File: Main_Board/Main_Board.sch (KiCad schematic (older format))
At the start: 67 parts, among them J1 Conn_01x06, J10 HR-SR04_L_CONN, J11 12V_OUT, J12 BATT_REG_IN, J13 LED_CONN, J14 PD_CONN, J2 Conn_01x06, J3 Conn_01x06, J4 BATT_IN, J5 Conn_02x08_Top_Bottom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

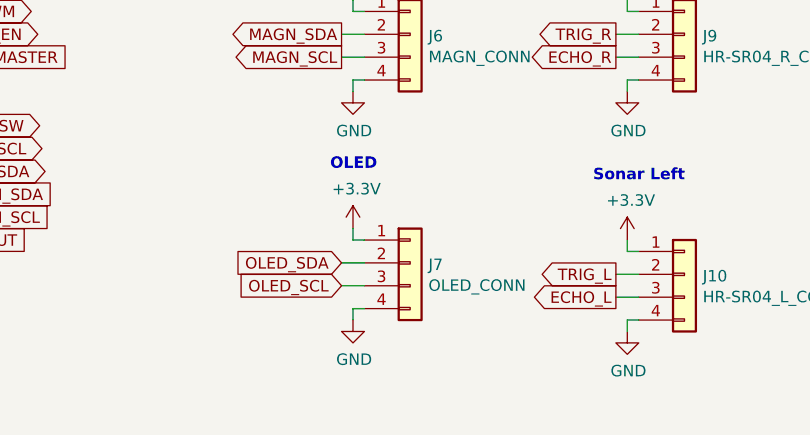
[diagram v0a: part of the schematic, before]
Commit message: Small changes to 12V connector [MAIN BOARD]
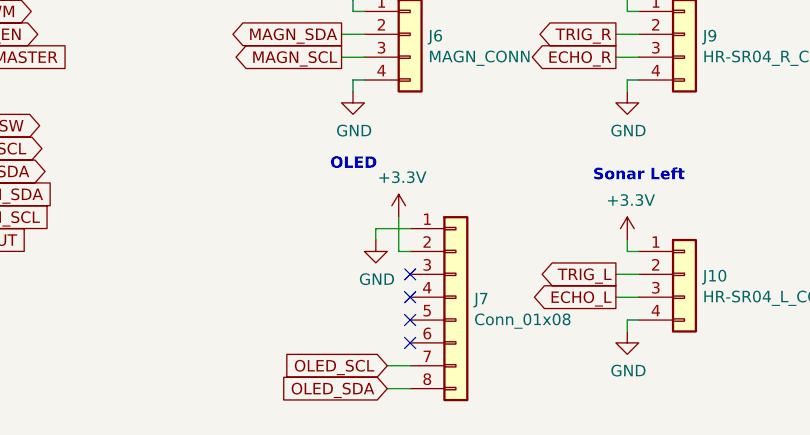
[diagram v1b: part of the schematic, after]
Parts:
- removed J7: OLED_CONN, Connector_PinSocket_2.54mm:PinSocket_1x04_P2.54mm_Vertical, symbol Connector_Generic:Conn_01x04
- added J7: Conn_01x08, symbol Connector_Generic:Conn_01x08
- J11, J12: footprint Connector_Molex:Molex_Mini-Fit_Jr_5566-04A_2x02_P4.20mm_Vertical -> Main_Board:215760-YY04
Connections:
- net +3V3: now also J7.2 (Pin_2)
- net GND: now also J7.1 (Pin_1)
- net OLED_SCL: now also J7.7 (Pin_7)
- net OLED_SDA: now also J7.8 (Pin_8)
- no-connect marks 93 -> 97
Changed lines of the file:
@@
-	1    0    0    -1
-$EndComp
-$Comp
-L Connector_Generic:Conn_01x04 J7
-U 1 1 61EF5837
-P 8500 10200
-F 0 "J7" H 8580 10192 50  0000 L CNN
-F 1 "OLED_CONN" H 8580 10101 50  0000 L CNN
-F 2 "Connector_PinSocket_2.54mm:PinSocket_1x04_P2.54mm_Vertical" H 8500 10200 50  0001 C CNN
-F 3 "~" H 8500 10200 50  0001 C CNN
-	1    8500 10200
 	1    0    0    -1
 $EndComp
@@
 Text GLabel 4550 8400 0    50   Output ~ 0
 LED_DIN
-Text GLabel 8200 10200 0    50   Input ~ 0
+Text GLabel 8400 10750 0    50   Input ~ 0
 OLED_SDA
-Text GLabel 8200 10300 0    50   Input ~ 0
+Text GLabel 8400 10650 0    50   Input ~ 0
 OLED_SCL
 Wire Wire Line
-	8200 10200 8300 10200
-Wire Wire Line
-	8200 10300 8300 10300
-Wire Wire Line
-	8250 10050 8250 10100
-Wire Wire Line
-	8250 10100 8300 10100
+	8400 10750 8500 10750
+Wire Wire Line
+	8400 10650 8500 10650
 $Comp
 L power:GND #PWR021
 U 1 1 620F9588
-P 8250 10450
-F 0 "#PWR021" H 8250 10200 50  0001 C CNN
-F 1 "GND" H 8255 10277 50  0000 C CNN
-F 2 "" H 8250 10450 50  0001 C CNN
-F 3 "" H 8250 10450 50  0001 C CNN
-	1    8250 10450
-	1    0    0    -1
-$EndComp
-Wire Wire Line
-	8250 10450 8250 10400
-Wire Wire Line
-	8250 10400 8300 10400
+P 8350 10100
+F 0 "#PWR021" H 8350 9850 50  0001 C CNN
+F 1 "GND" H 8355 9927 50  0000 C CNN
+F 2 "" H 8350 10100 50  0001 C CNN
+F 3 "" H 8350 10100 50  0001 C CNN
+	1    8350 10100
+	1    0    0    -1
+$EndComp
+Wire Wire Line
+	8350 10100 8350 10050
+Wire Wire Line
+	8350 10050 8500 10050
 Text GLabel 8200 9200 0    50   Output ~ 0
 MAGN_SDA
@@
 L power:+3.3V #PWR020
 U 1 1 62001B8E
-P 8250 10050
-F 0 "#PWR020" H 8250 9900 50  0001 C CNN
-F 1 "+3.3V" H 8265 10223 50  0000 C CNN
-F 2 "" H 8250 10050 50  0001 C CNN
-F 3 "" H 8250 10050 50  0001 C CNN
-	1    8250 10050
+P 8450 10000
+F 0 "#PWR020" H 8450 9850 50  0001 C CNN
+F 1 "+3.3V" H 8465 10173 50  0000 C CNN
+F 2 "" H 8450 10000 50  0001 C CNN
+F 3 "" H 8450 10000 50  0001 C CNN
+	1    8450 10000
 	1    0    0    -1
 $EndComp
@@
 F 0 "J11" H 7750 2000 50  0000 L CNN
 F 1 "12V_OUT" H 7650 1700 50  0000 L CNN
-F 2 "Connector_Molex:Molex_Mini-Fit_Jr_5566-04A_2x02_P4.20mm_Vertical" H 7800 1900 50  0001 C CNN
+F 2 "Main_Board:215760-YY04" H 7800 1900 50  0001 C CNN
 F 3 "~" H 7800 1900 50  0001 C CNN
 	1    7800 1900
@@
 F 0 "J12" H 8200 1700 50  0000 L CNN
 F 1 "BATT_REG_IN" H 8100 2000 50  0000 L CNN
-F 2 "Connector_Molex:Molex_Mini-Fit_Jr_5566-04A_2x02_P4.20mm_Vertical" H 8250 1900 50  0001 C CNN
+F 2 "Main_Board:215760-YY04" H 8250 1900 50  0001 C CNN
 F 3 "~" H 8250 1900 50  0001 C CNN
 	1    8250 1900
@@
 Wire Wire Line
 	12100 8150 12200 8150
+$Comp
+L Connector_Generic:Conn_01x08 J7
+U 1 1 6204F2B5
+P 8700 10350
+F 0 "J7" H 8780 10342 50  0000 L CNN
+F 1 "Conn_01x08" H 8780 10251 50  0000 L CNN
+F 2 "" H 8700 10350 50  0001 C CNN
+F 3 "~" H 8700 10350 50  0001 C CNN
+	1    8700 10350
+	1    0    0    -1
+$EndComp
+NoConn ~ 8500 10550
+NoConn ~ 8500 10450
+NoConn ~ 8500 10350
+NoConn ~ 8500 10250
+Wire Wire Line
+	8500 10150 8450 10150
+Wire Wire Line
+	8450 10150 8450 10000
 $EndSCHEMATC

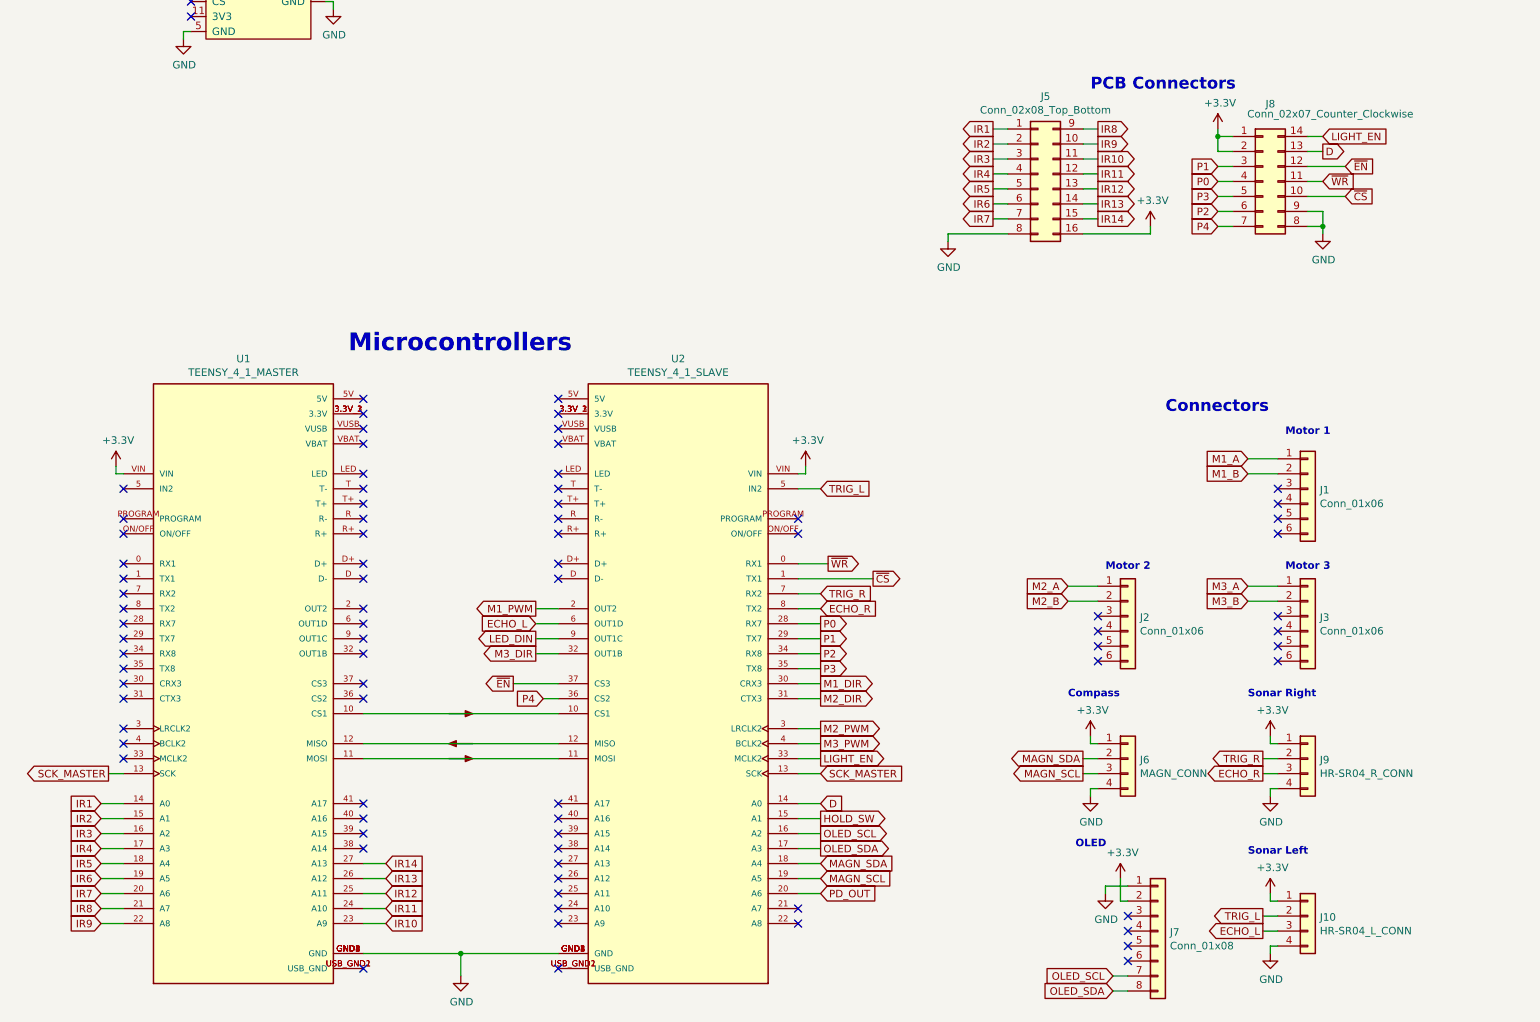
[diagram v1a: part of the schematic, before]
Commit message: Started actual traces [MAIN BOARD]
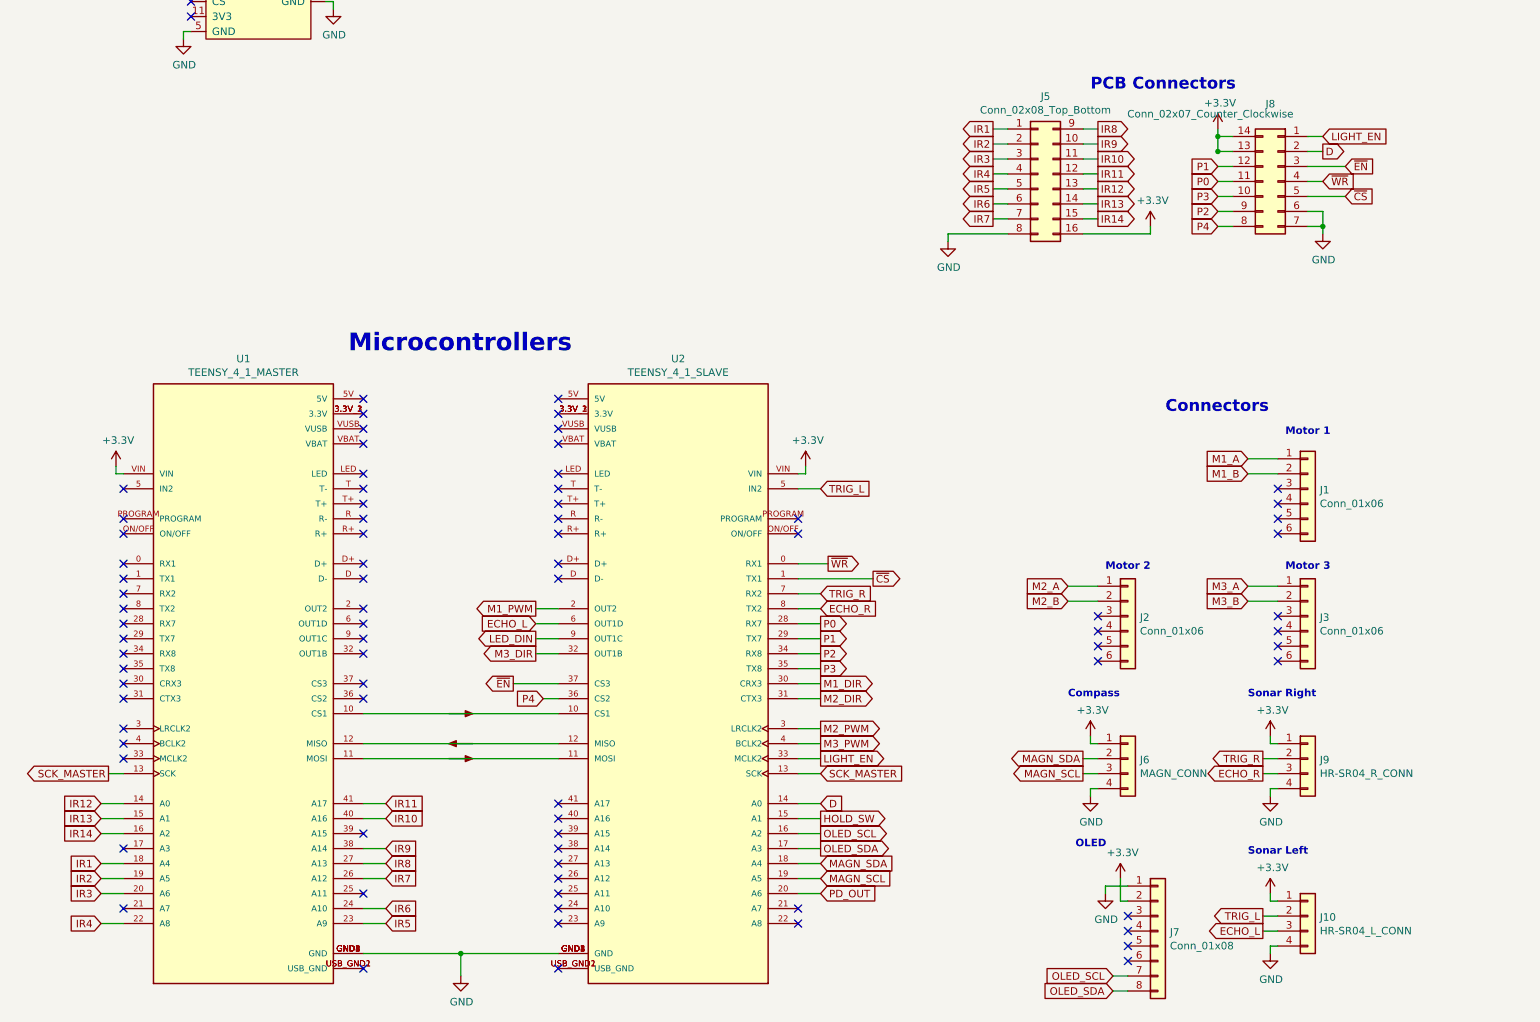
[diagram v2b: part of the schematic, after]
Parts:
- J7: footprint (none) -> Connector_PinSocket_2.54mm:PinSocket_1x08_P2.54mm_Vertical
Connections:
- net +3V3: now also J8.13 (Pin_13), J8.14 (Pin_14); no longer J8.1 (Pin_1), J8.2 (Pin_2)
- net D: now also J8.2 (Pin_2); no longer J8.13 (Pin_13)
- net GND: now also J8.6 (Pin_6), J8.7 (Pin_7); no longer J8.8 (Pin_8), J8.9 (Pin_9)
- net IR1: now also U1.18 (A4); no longer U1.14 (A0)
- net IR10: now also U1.40 (A16); no longer U1.23 (A9)
- net IR11: now also U1.41 (A17); no longer U1.24 (A10)
- net IR12: now also U1.14 (A0); no longer U1.25 (A11)
- net IR13: now also U1.15 (A1); no longer U1.26 (A12)
- net IR14: now also U1.16 (A2); no longer U1.27 (A13)
- net IR2: now also U1.19 (A5); no longer U1.15 (A1)
- net IR3: now also U1.20 (A6); no longer U1.16 (A2)
- net IR4: now also U1.22 (A8); no longer U1.17 (A3)
- net IR5: now also U1.23 (A9); no longer U1.18 (A4)
- net IR6: now also U1.24 (A10); no longer U1.19 (A5)
- net IR7: now also U1.26 (A12); no longer U1.20 (A6)
- net IR8: now also U1.27 (A13); no longer U1.21 (A7)
- net IR9: now also U1.38 (A14); no longer U1.22 (A8)
- net LIGHT_EN: now also J8.1 (Pin_1); no longer J8.14 (Pin_14)
- net P0: now also J8.11 (Pin_11); no longer J8.4 (Pin_4)
- net P1: now also J8.12 (Pin_12); no longer J8.3 (Pin_3)
- net P2: now also J8.9 (Pin_9); no longer J8.6 (Pin_6)
- net P3: now also J8.10 (Pin_10); no longer J8.5 (Pin_5)
- net P4: now also J8.8 (Pin_8); no longer J8.7 (Pin_7)
- net ~CS: now also J8.5 (Pin_5); no longer J8.10 (Pin_10)
- net ~EN: now also J8.3 (Pin_3); no longer J8.12 (Pin_12)
- net ~WR: now also J8.4 (Pin_4); no longer J8.11 (Pin_11)
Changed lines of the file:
@@
 Wire Wire Line
 	4700 10500 4050 10500
-$Comp
-L TEENSY_4_1:TEENSY_4_1 U1
-U 1 1 61B35EEE
-P 2600 8700
-F 0 "U1" H 2600 10867 50  0000 C CNN
-F 1 "TEENSY_4_1_MASTER" H 2600 10776 50  0000 C CNN
-F 2 "Main_Board:TEENSY_4_1_FP" H 2600 8700 50  0001 L BNN
-F 3 "" H 2600 8700 50  0001 L BNN
-F 4 "Manufacturer recommendations" H 2600 8700 50  0001 L BNN "STANDARD"
-F 5 "4.07mm" H 2600 8700 50  0001 L BNN "MAXIMUM_PACKAGE_HEIGHT"
-F 6 "4.1" H 2600 8700 50  0001 L BNN "PARTREV"
-F 7 "SparkFun Electronics" H 2600 8700 50  0001 L BNN "MANUFACTURER"
-	1    2600 8700
-	1    0    0    -1
-$EndComp
 Wire Wire Line
 	6300 7300 6350 7300
@@
 NoConn ~ 3400 7100
 NoConn ~ 4700 7100
-$Comp
-L Connector_Generic:Conn_02x07_Counter_Clockwise J8
-U 1 1 62B05C9E
-P 9400 5350
-F 0 "J8" H 9450 5867 50  0000 C CNN
-F 1 "Conn_02x07_Counter_Clockwise" H 9850 5800 50  0000 C CNN
-F 2 "Connector_Hirose:Hirose_DF11-14DP-2DSA_2x07_P2.00mm_Vertical" H 9400 5350 50  0001 C CNN
-F 3 "~" H 9400 5350 50  0001 C CNN
-	1    9400 5350
-	1    0    0    -1
-$EndComp
 Text GLabel 9100 5350 0    50   Input ~ 0
 P0
@@
 Wire Wire Line
 	6450 8200 6300 8200
+Text GLabel 1650 9700 0    50   Input ~ 0
+IR14
+Text GLabel 1650 9600 0    50   Input ~ 0
+IR13
+Text GLabel 1650 9500 0    50   Input ~ 0
+IR12
+Text GLabel 3550 9500 2    50   Input ~ 0
+IR11
+Text GLabel 3550 9600 2    50   Input ~ 0
+IR10
+Text GLabel 3550 9800 2    50   Input ~ 0
+IR9
 Text GLabel 3550 9900 2    50   Input ~ 0
-IR14
+IR8
 Text GLabel 3550 10000 2    50   Input ~ 0
-IR13
-Text GLabel 3550 10100 2    50   Input ~ 0
-IR12
+IR7
 Text GLabel 3550 10200 2    50   Input ~ 0
-IR11
+IR6
 Text GLabel 3550 10300 2    50   Input ~ 0
-IR10
-Text GLabel 1650 10300 0    50   Input ~ 0
-IR9
-Text GLabel 1650 10200 0    50   Input ~ 0
-IR8
+IR5
 Text GLabel 1650 10100 0    50   Input ~ 0
-IR7
+IR3
 Text GLabel 1650 10000 0    50   Input ~ 0
-IR6
+IR2
 Text GLabel 1650 9900 0    50   Input ~ 0
-IR5
-Text GLabel 1650 9800 0    50   Input ~ 0
-IR4
-Text GLabel 1650 9700 0    50   Input ~ 0
-IR3
-Text GLabel 1650 9600 0    50   Input ~ 0
-IR2
-Text GLabel 1650 9500 0    50   Input ~ 0
 IR1
 Wire Wire Line
@@
 	1650 9700 1800 9700
 Wire Wire Line
-	1650 9800 1800 9800
-Wire Wire Line
-	1650 9900 1800 9900
-Wire Wire Line
 	1650 10000 1800 10000
 Wire Wire Line
 	1650 10100 1800 10100
 Wire Wire Line
-	1650 10200 1800 10200
-Wire Wire Line
 	1650 10300 1800 10300
 Wire Wire Line
@@
 Wire Wire Line
 	3550 10200 3400 10200
-Wire Wire Line
-	3550 10100 3400 10100
 Wire Wire Line
 	3550 10000 3400 10000
@@
 NoConn ~ 4700 7900
 NoConn ~ 4700 8000
-NoConn ~ 3400 9500
-NoConn ~ 3400 9600
-NoConn ~ 3400 9700
-NoConn ~ 3400 9800
 $Comp
 L Connector_Generic:Conn_02x08_Top_Bottom J5
@@
 F 0 "J7" H 8780 10342 50  0000 L CNN
 F 1 "Conn_01x08" H 8780 10251 50  0000 L CNN
-F 2 "" H 8700 10350 50  0001 C CNN
+F 2 "Connector_PinSocket_2.54mm:PinSocket_1x08_P2.54mm_Vertical" H 8700 10350 50  0001 C CNN
 F 3 "~" H 8700 10350 50  0001 C CNN
 	1    8700 10350
@@
 Wire Wire Line
 	8450 10150 8450 10000
+Wire Wire Line
+	3550 9500 3400 9500
+$Comp
+L TEENSY_4_1:TEENSY_4_1 U1
+U 1 1 61B35EEE
+P 2600 8700
+F 0 "U1" H 2600 10867 50  0000 C CNN
+F 1 "TEENSY_4_1_MASTER" H 2600 10776 50  0000 C CNN
+F 2 "Main_Board:TEENSY_4_1_FP" H 2600 8700 50  0001 L BNN
+F 3 "" H 2600 8700 50  0001 L BNN
+F 4 "Manufacturer recommendations" H 2600 8700 50  0001 L BNN "STANDARD"
+F 5 "4.07mm" H 2600 8700 50  0001 L BNN "MAXIMUM_PACKAGE_HEIGHT"
+F 6 "4.1" H 2600 8700 50  0001 L BNN "PARTREV"
+F 7 "SparkFun Electronics" H 2600 8700 50  0001 L BNN "MANUFACTURER"
+	1    2600 8700
+	1    0    0    -1
+$EndComp
+Wire Wire Line
+	1650 9900 1800 9900
+Text GLabel 1650 10300 0    50   Input ~ 0
+IR4
+Wire Wire Line
+	3550 9600 3400 9600
+Wire Wire Line
+	3550 9800 3400 9800
+NoConn ~ 1800 9800
+NoConn ~ 1800 10200
+NoConn ~ 3400 10100
+NoConn ~ 3400 9700
+$Comp
+L Connector_Generic:Conn_02x07_Counter_Clockwise J8
+U 1 1 62B05C9E
+P 9500 5350
+F 0 "J8" H 9550 5867 50  0000 C CNN
+F 1 "Conn_02x07_Counter_Clockwise" H 9950 5800 50  0000 C CNN
+F 2 "Connector_Hirose:Hirose_DF11-14DP-2DSA_2x07_P2.00mm_Vertical" H 9500 5350 50  0001 C CNN
+F 3 "~" H 9500 5350 50  0001 C CNN
+	1    9500 5350
+	-1   0    0    -1
+$EndComp
+Connection ~ 9100 5150
 $EndSCHEMATC
